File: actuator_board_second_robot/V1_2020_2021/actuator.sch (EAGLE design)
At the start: 35 parts, among them CON1 SM03B-GHS-TB, CON2 SM03B-GHS-TB, CON3 MOLEX_5566-2, Q3 IRL6372TRPBF, Q4 IRL6372TRPBF, U3 TCAN1042HVDR, U4 PCA9685PW, U5 TEENSY_3.1_BASIC_2, X1 OSTVN05A150, X2 MOLEX_5566-4

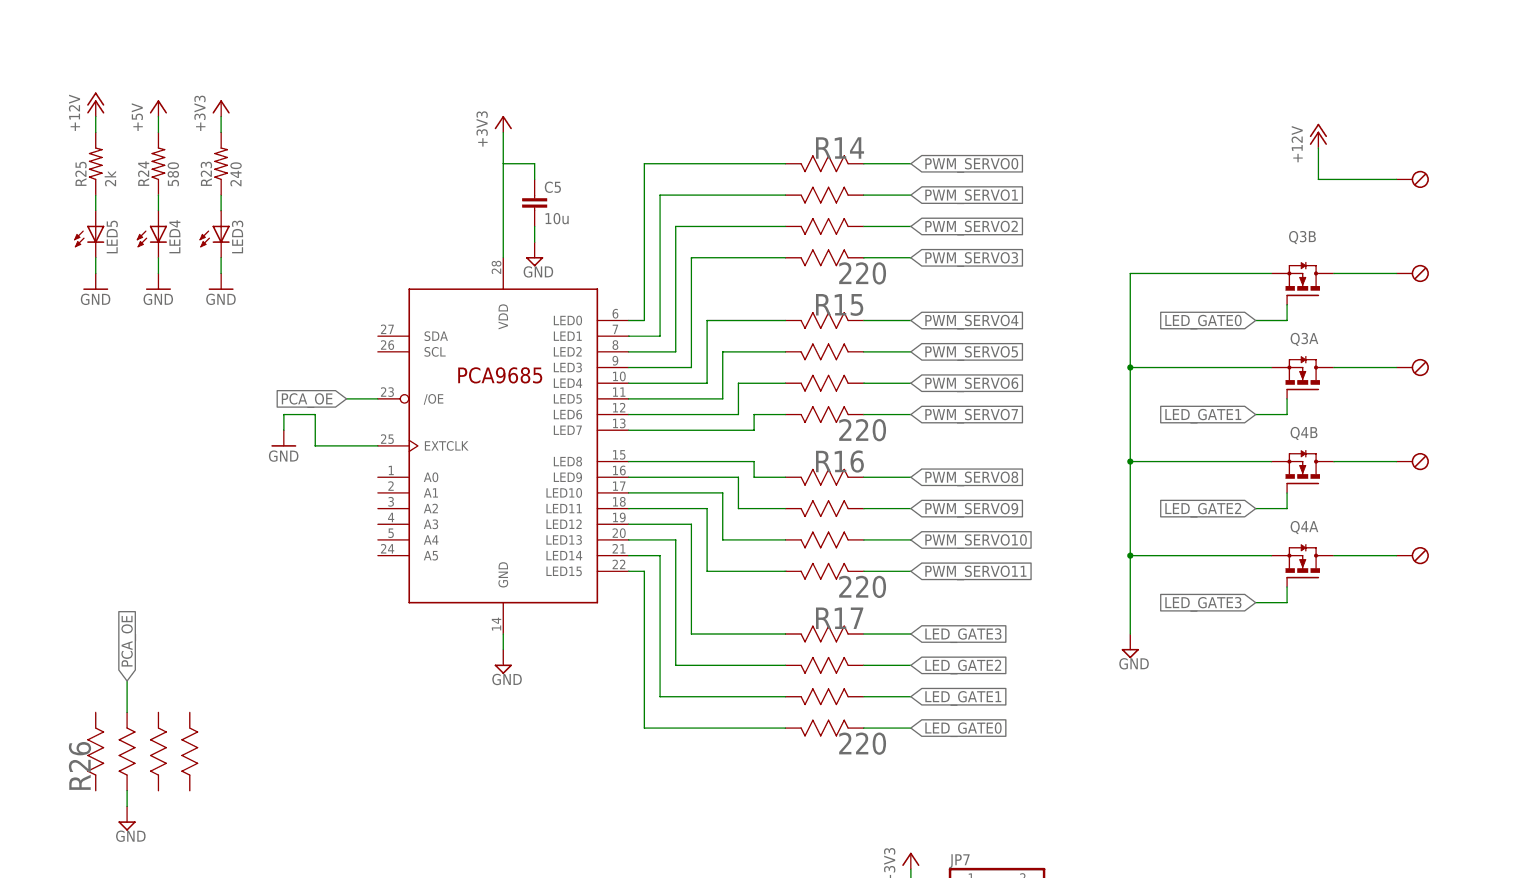
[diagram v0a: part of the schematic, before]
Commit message: Removed LED components
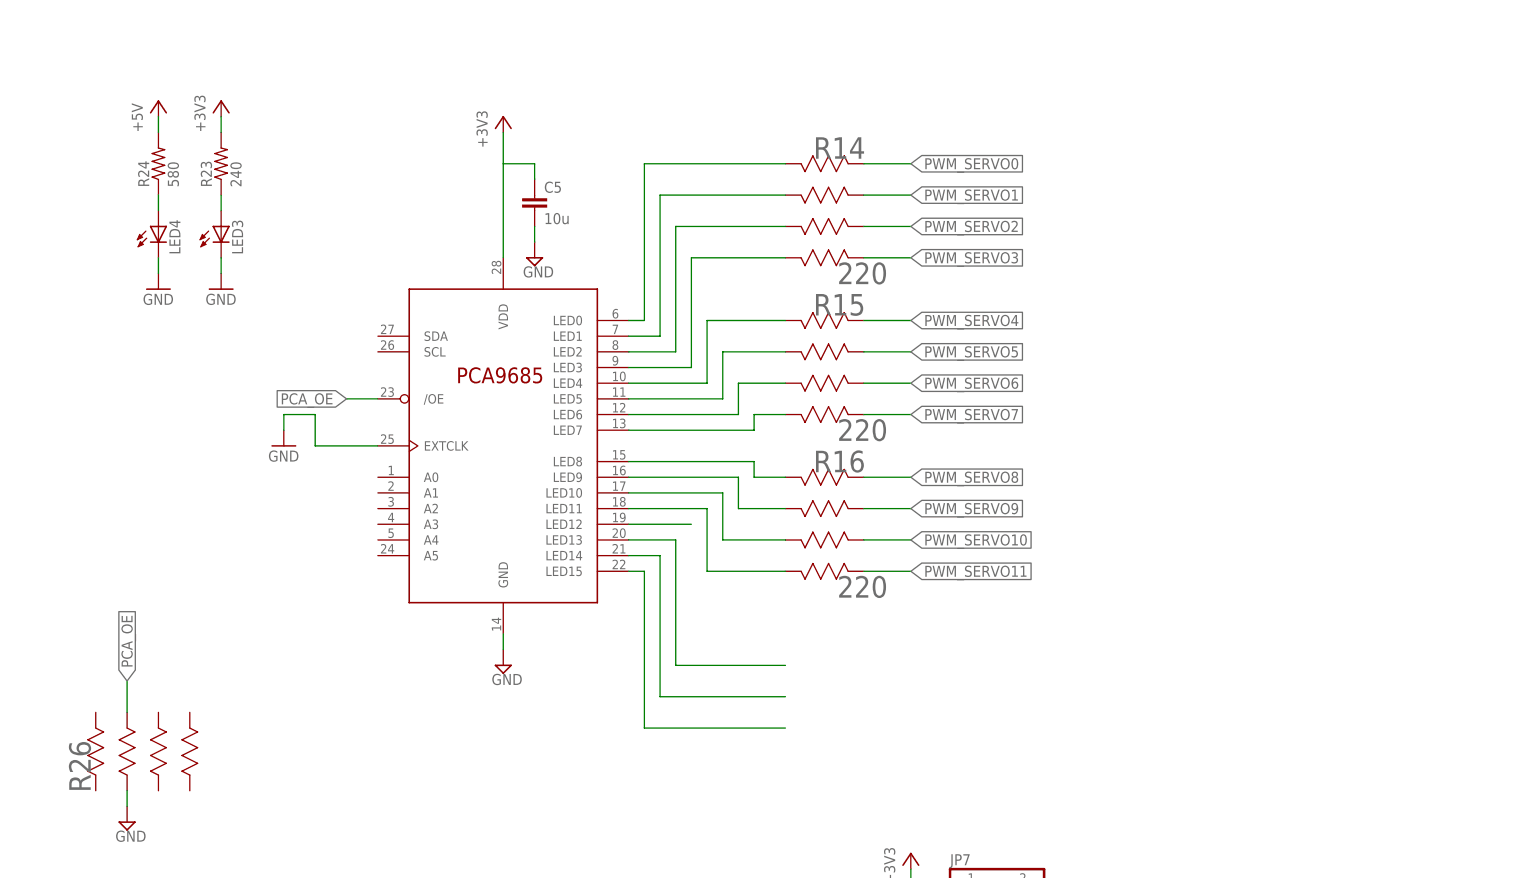
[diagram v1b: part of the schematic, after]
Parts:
- removed LED5: (no value), led:LEDCHIPLED_1206
- removed Q3, Q4: IRL6372TRPBF, dropper_torpedo_v3:IRL6372TRPBF
- removed R17: 220, ARVP:EXB-V8V221JVEXBV8V-M
- removed R25: 2k, rcl:R-US_R1206
- removed X1: OSTVN05A150, dropper_torpedo_v3:OSTVN05A150
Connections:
- removed net LED_DRAIN0: Q3B.D, X1G$4.1
- removed net LED_DRAIN1: Q3A.D, X1G$3.1
- removed net LED_DRAIN2: Q4B.D, X1G$2.1
- removed net LED_DRAIN3: Q4A.D, X1G$1.1
- removed net LED_GATE0: Q3B.G, R17.47
- removed net LED_GATE1: Q3A.G, R17.35
- removed net LED_GATE2: Q4B.G, R17.23
- removed net LED_GATE3: Q4A.G, R17.11
- removed net N$5: LED5.A, R25.1
- removed net PWM_CH12: R17.82, U4.LED12
- new net N$1: U4.LED12
- net +12V: no longer R25.2, X1G$5.1
- net GND: no longer LED5.C, Q3A.S, Q3B.S, Q4A.S, Q4B.S
- net PWM_CH13: no longer R17.74
- net PWM_CH14: no longer R17.66
- net PWM_CH15: no longer R17.58

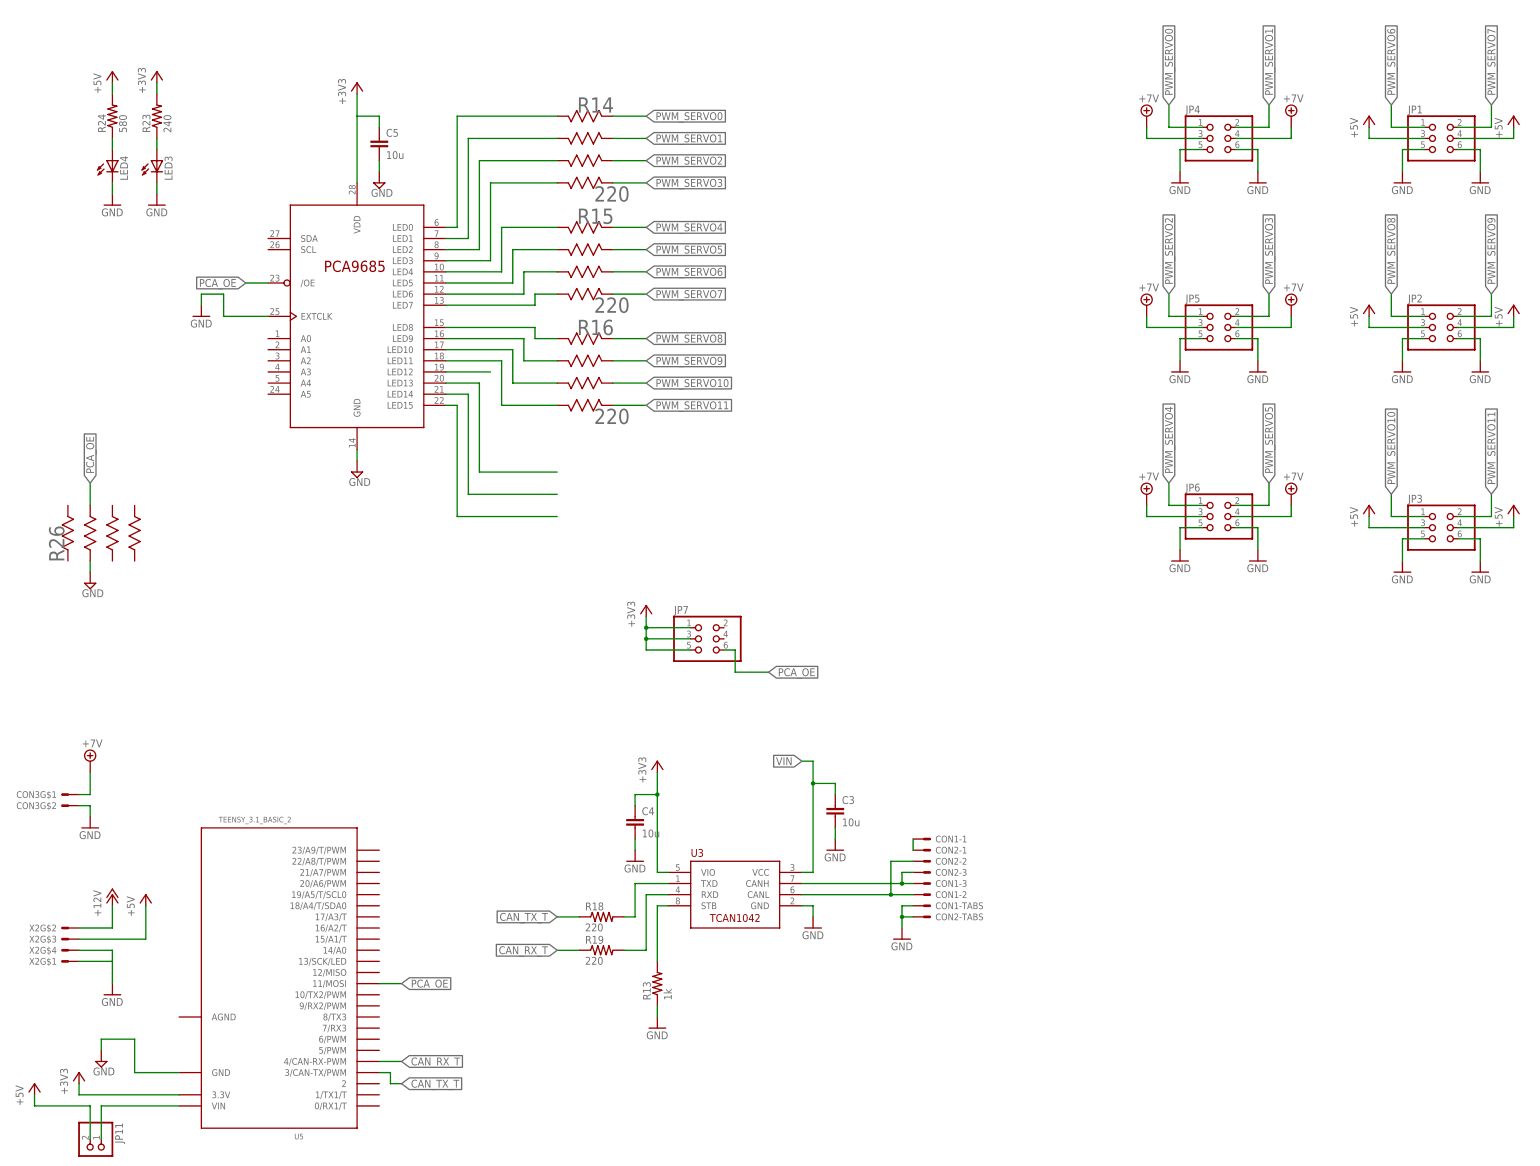
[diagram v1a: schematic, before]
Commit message: Removed 5V servo channels, changed one to 7V.
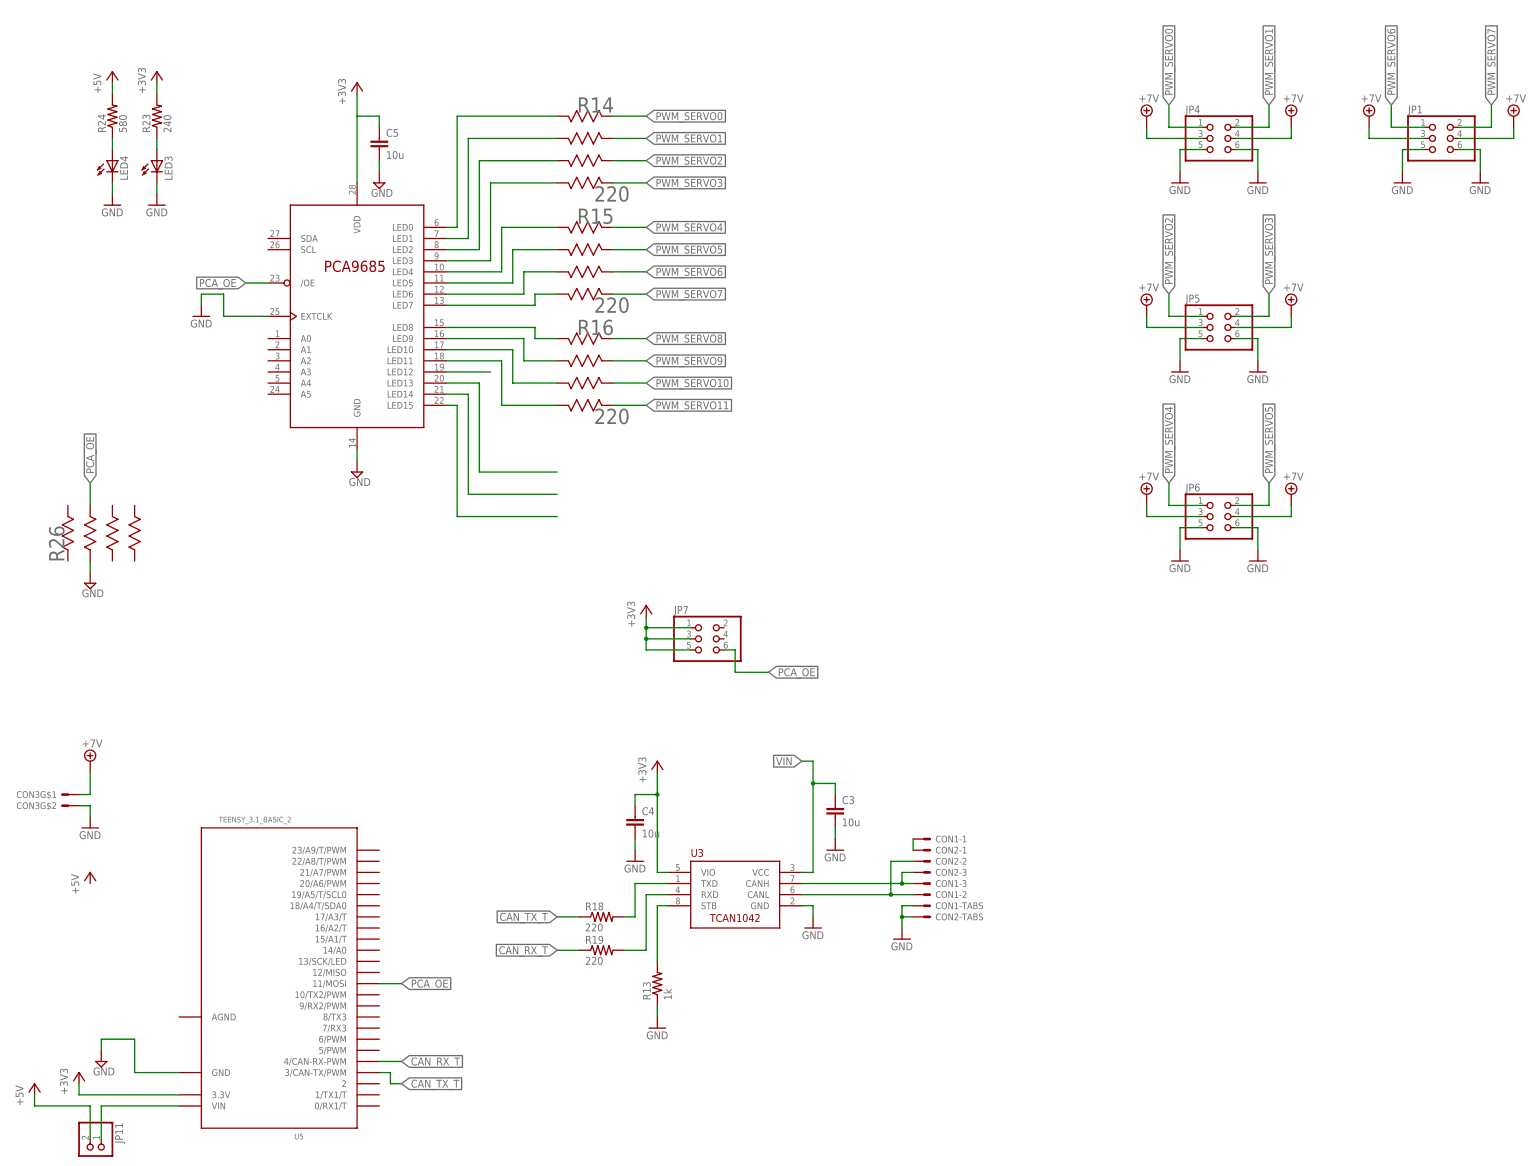
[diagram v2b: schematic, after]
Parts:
- removed JP2, JP3: (no value), pinhead:PINHD-2X3
- removed X2: MOLEX_5566-4, ARVP:MOLEX_5566-4
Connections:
- removed net +12V: X2G$2.S
- net +5V: no longer JP1.3, JP1.4, JP2.3, JP2.4, JP3.3, JP3.4, X2G$3.S
- net +7V: now also JP1.3, JP1.4
- net GND: no longer JP2.5, JP2.6, JP3.5, JP3.6, X2G$1.S, X2G$4.S
- net PWM_SERVO10: no longer JP3.1
- net PWM_SERVO11: no longer JP3.2
- net PWM_SERVO8: no longer JP2.1
- net PWM_SERVO9: no longer JP2.2
